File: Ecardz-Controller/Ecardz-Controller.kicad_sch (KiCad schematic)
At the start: 0 parts

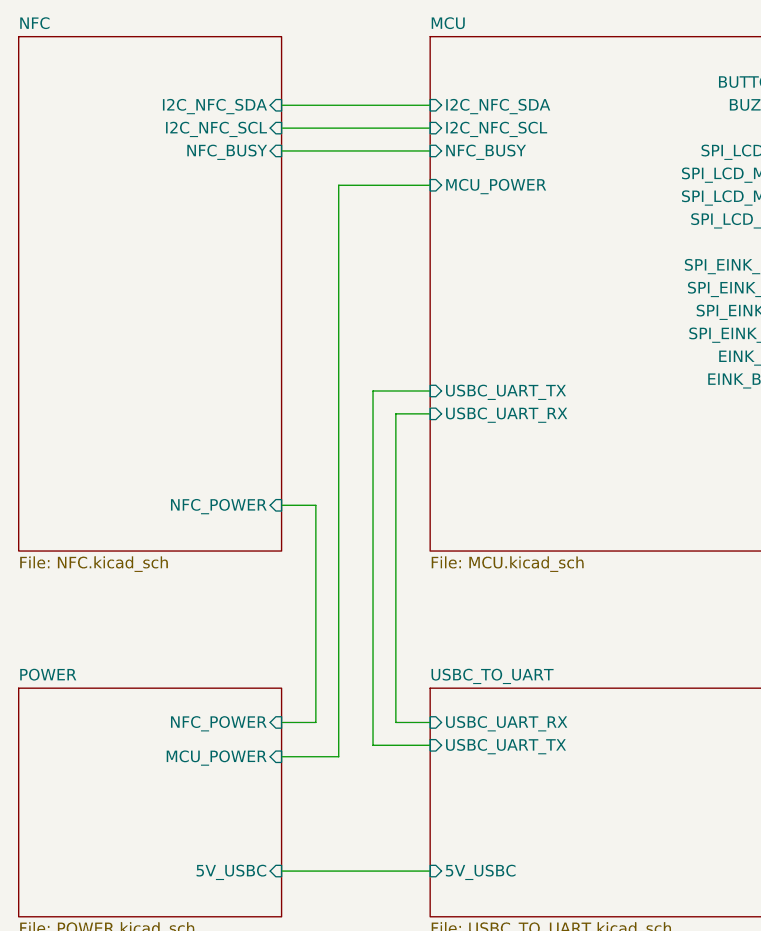
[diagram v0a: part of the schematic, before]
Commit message: updated button pin choices, updated root
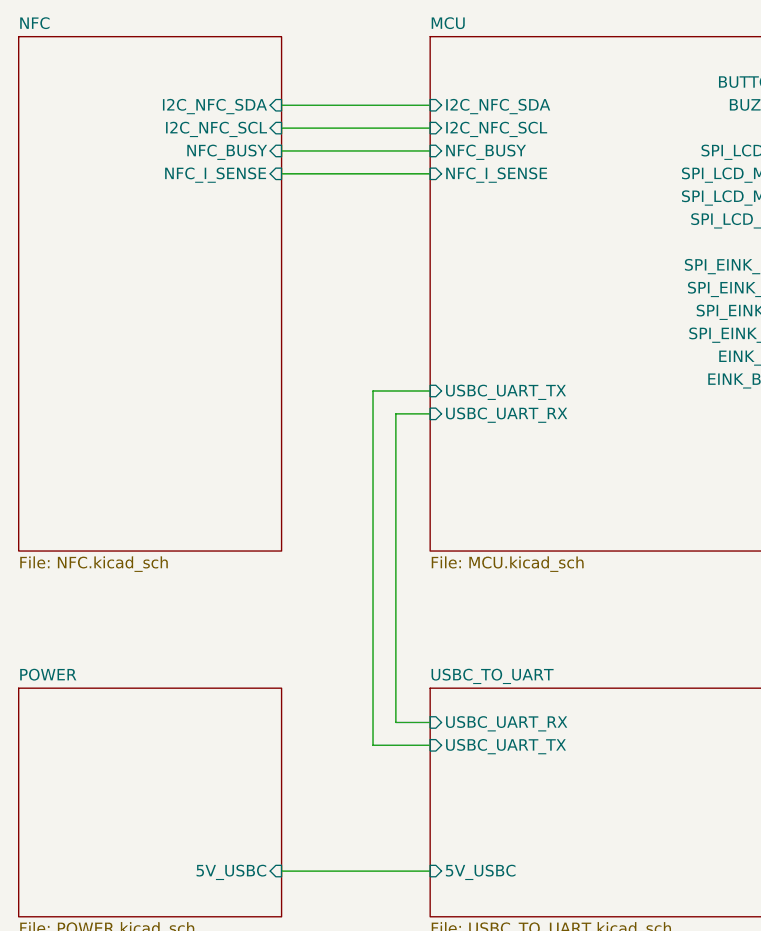
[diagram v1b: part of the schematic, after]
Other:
- sheet MCU ports: added NFC_I_SENSE; removed MCU_POWER
- sheet NFC ports: added NFC_I_SENSE; removed NFC_POWER
- sheet POWER ports: added none; removed MCU_POWER, NFC_POWER
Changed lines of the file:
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@@
-	(wire
-		(pts
-			(xy 92.71 127) (xy 92.71 102.87)
-		)
-		(stroke
-			(width 0)
-			(type default)
-		)
-	)
 	(wire
 		(pts
@@
 	(wire
 		(pts
-			(xy 88.9 127) (xy 92.71 127)
-		)
-		(stroke
-			(width 0)
-			(type default)
-		)
-	)
-	(wire
-		(pts
 			(xy 147.32 58.42) (xy 161.29 58.42)
 		)
@@
 	(wire
 		(pts
-			(xy 95.25 67.31) (xy 95.25 130.81)
-		)
-		(stroke
-			(width 0)
-			(type default)
-		)
-	)
-	(wire
-		(pts
 			(xy 147.32 78.74) (xy 161.29 78.74)
 		)
@@
 	(wire
 		(pts
-			(xy 95.25 130.81) (xy 88.9 130.81)
+			(xy 88.9 66.04) (xy 105.41 66.04)
 		)
 		(stroke
@@
 	(wire
 		(pts
-			(xy 92.71 102.87) (xy 88.9 102.87)
-		)
-		(stroke
-			(width 0)
-			(type default)
-		)
-	)
-	(wire
-		(pts
 			(xy 101.6 127) (xy 101.6 92.71)
-		)
-		(stroke
-			(width 0)
-			(type default)
-		)
-	)
-	(wire
-		(pts
-			(xy 105.41 67.31) (xy 95.25 67.31)
 		)
 		(stroke
@@
 			)
 		)
-		(pin "MCU_POWER" input
-			(at 105.41 67.31 180)
-			(effects
-				(font
-					(size 1.27 1.27)
-				)
-				(justify left)
-			)
-		)
 		(pin "SPI_LCD_CS" input
 			(at 147.32 63.5 0)
@@
 				)
 				(justify right)
+			)
+		)
+		(pin "NFC_I_SENSE" input
+			(at 105.41 66.04 180)
+			(effects
+				(font
+					(size 1.27 1.27)
+				)
+				(justify left)
 			)
 		)
@@
 			)
 		)
-		(pin "NFC_POWER" input
-			(at 88.9 102.87 0)
+		(pin "NFC_I_SENSE" input
+			(at 88.9 66.04 0)
 			(effects
 				(font
@@
 			(effects
 				(font
-					(size 1.27 1.27)
-				)
-				(justify right)
-			)
-		)
-		(pin "NFC_POWER" input
-			(at 88.9 127 0)
-			(effects
-				(font
-					(size 1.27 1.27)
-				)
-				(justify right)
-			)
-		)
-		(pin "MCU_POWER" input
-			(at 88.9 130.81 0)
-			(effects
-				(font

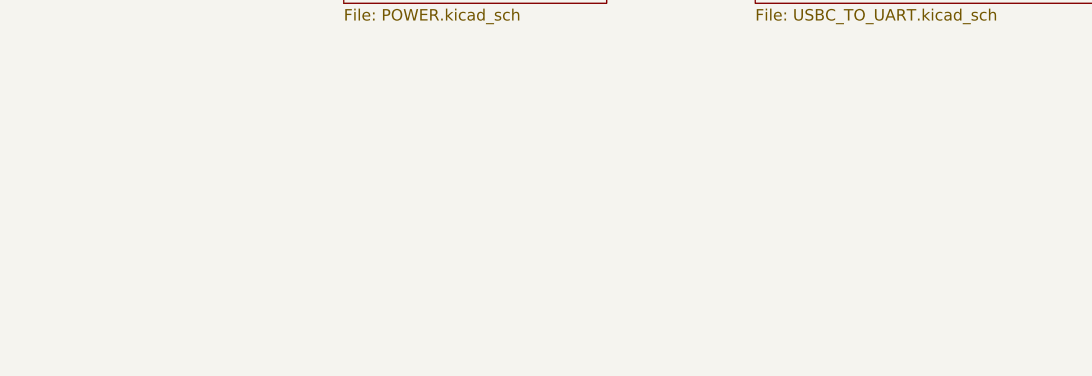
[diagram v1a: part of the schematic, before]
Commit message: added eink and lcd pinouts
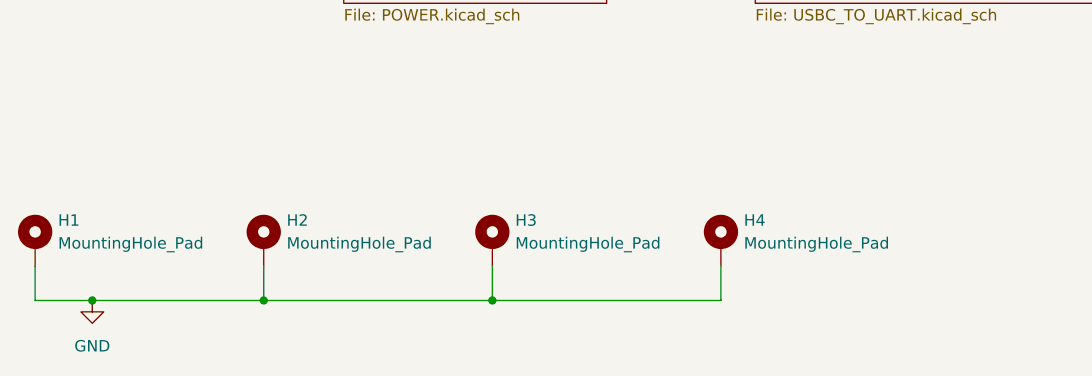
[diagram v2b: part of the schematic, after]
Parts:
- added H1, H2, H3, H4: MountingHole_Pad, symbol Mechanical:MountingHole_Pad
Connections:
- new net GND: H1.1, H2.1, H3.1, H4.1

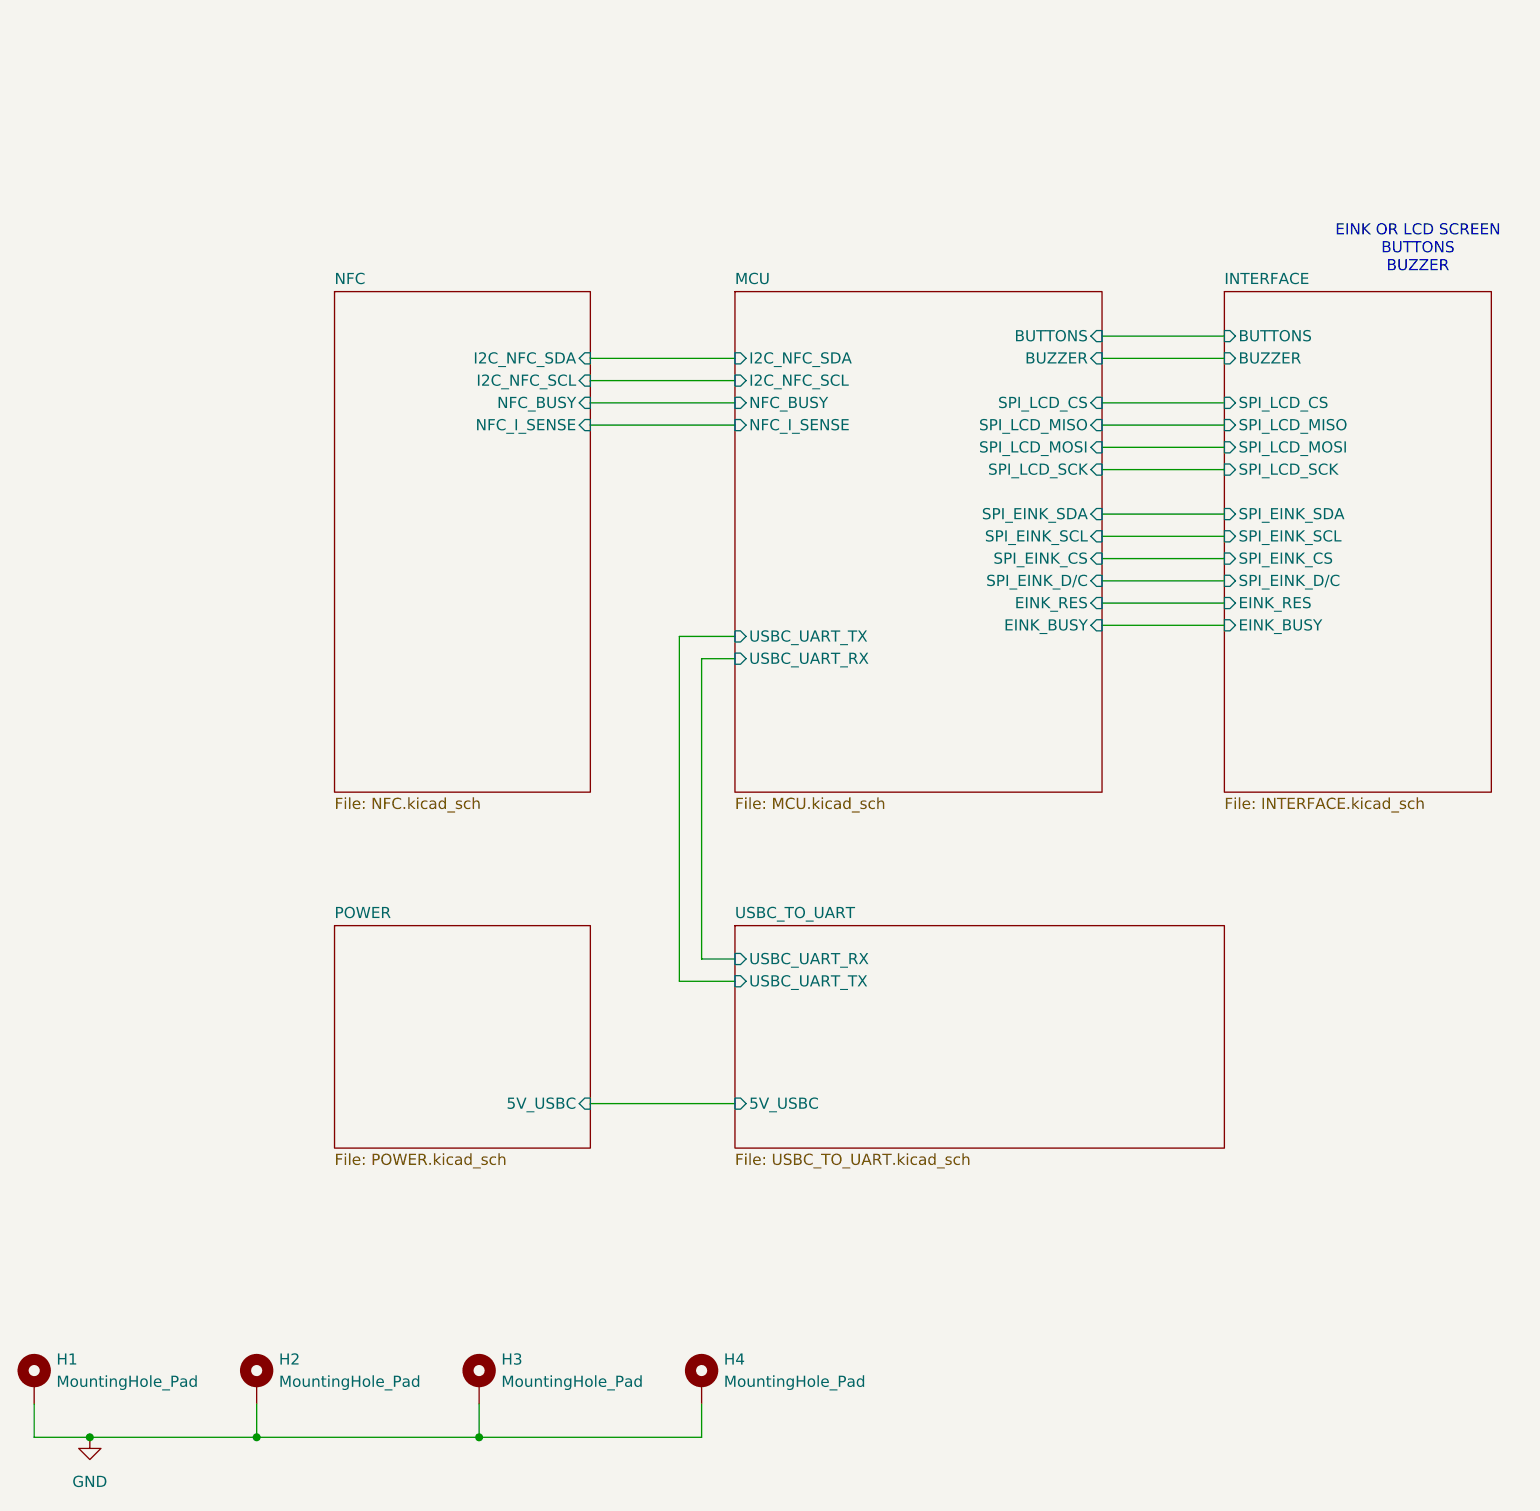
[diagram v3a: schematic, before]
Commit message: did bulk of controller layout apart from the antenna, added some NCs and other minor clean ups on schematic
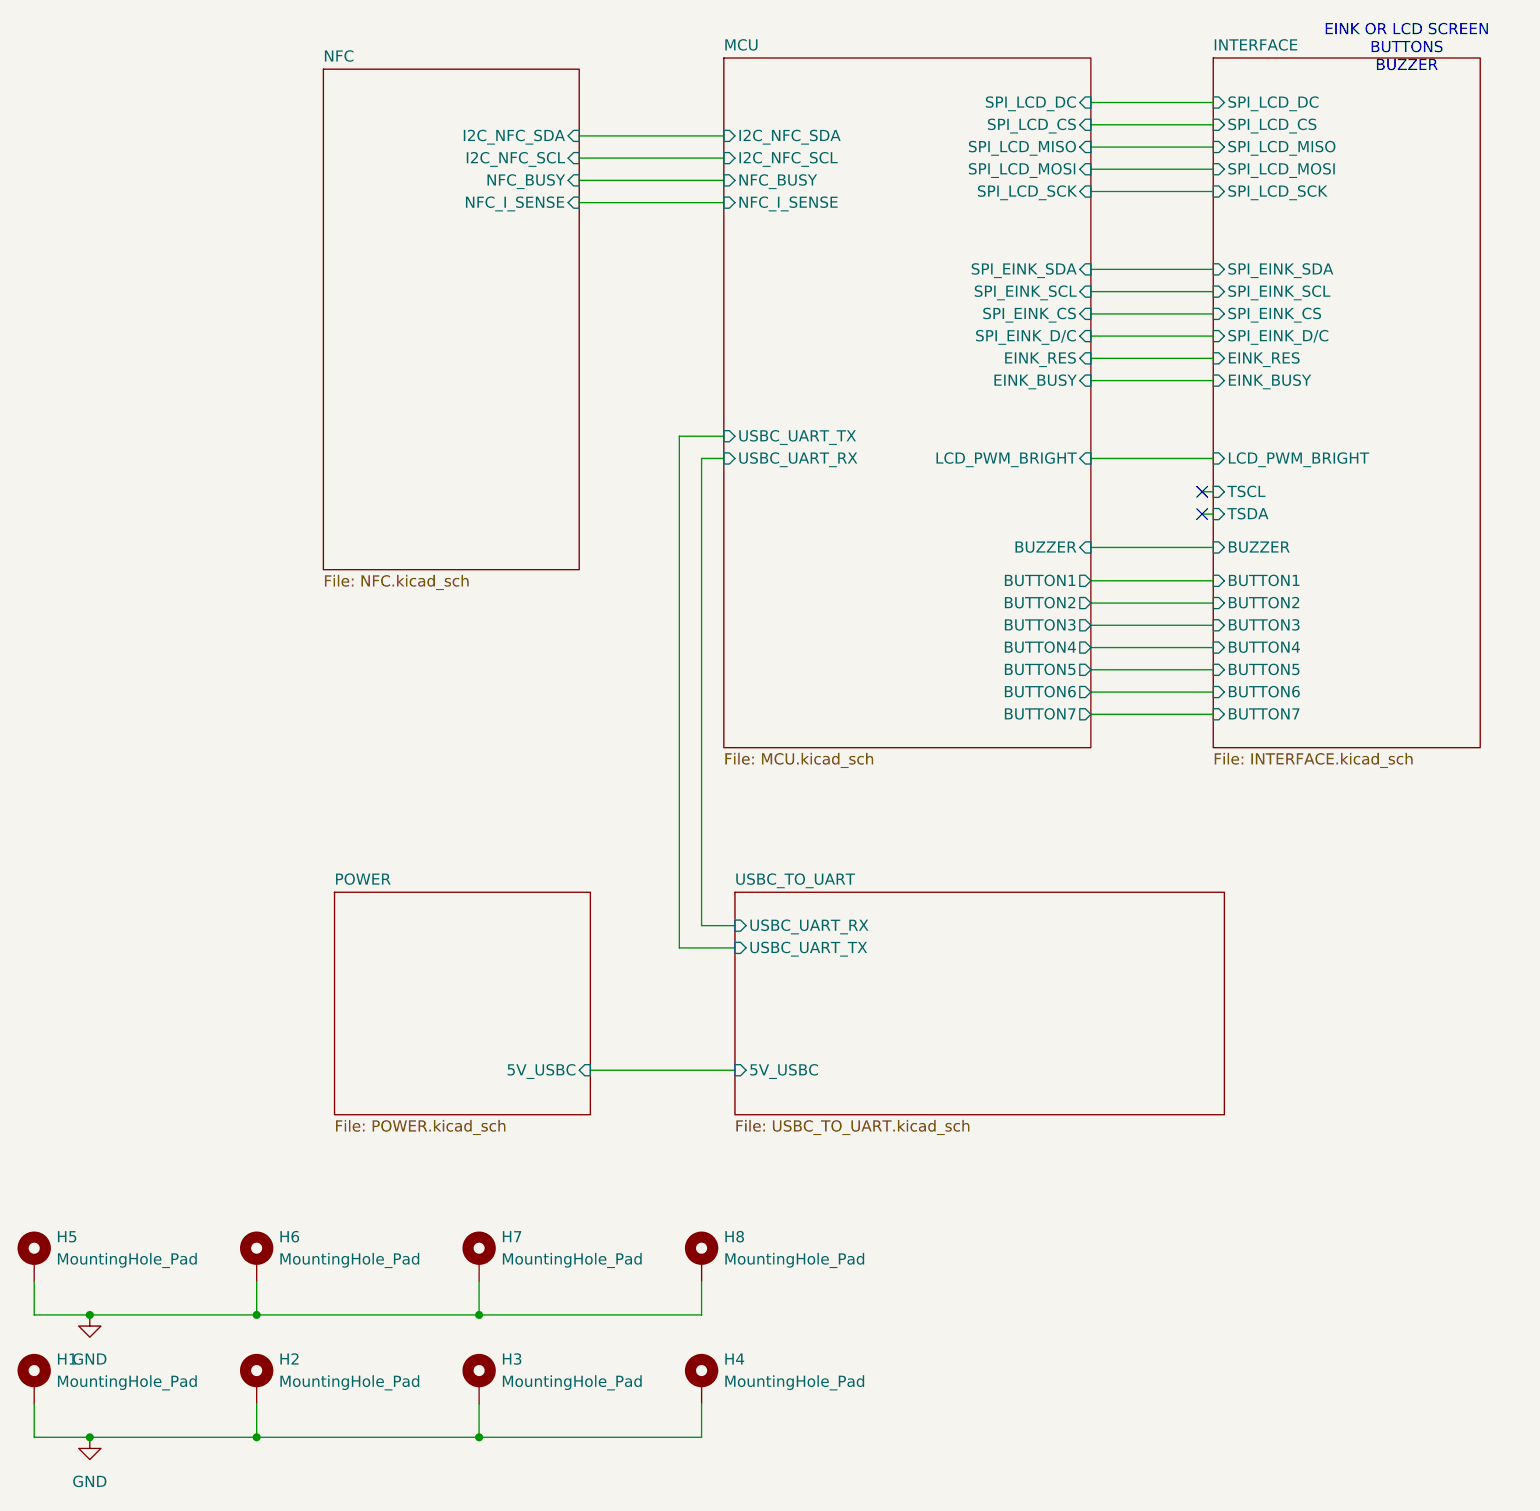
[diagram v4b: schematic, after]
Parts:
- added H5, H6, H7, H8: MountingHole_Pad, MountingHole:MountingHole_2.7mm_M2.5_Pad_TopBottom, symbol Mechanical:MountingHole_Pad
- H1, H2, H3, H4: footprint (none) -> MountingHole:MountingHole_2.7mm_M2.5_Pad_TopBottom
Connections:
- net GND: now also H5.1, H6.1, H7.1, H8.1
- no-connect marks 0 -> 2
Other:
- sheet INTERFACE ports: added BUTTON1, BUTTON2, BUTTON3, BUTTON4, BUTTON5, BUTTON6, BUTTON7, LCD_PWM_BRIGHT, SPI_LCD_DC, TSCL, TSDA; removed BUTTONS
- sheet MCU ports: added BUTTON1, BUTTON2, BUTTON3, BUTTON4, BUTTON5, BUTTON6, BUTTON7, LCD_PWM_BRIGHT, SPI_LCD_DC; removed BUTTONS
